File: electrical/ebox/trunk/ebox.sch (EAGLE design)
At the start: 160 parts, among them IC1 MAX3221CUE, IC10 SN74LVC1G125, IC11 MAX3221CUE, IC12 INA170, IC13 SN74LVC1G125, IC14 SN74LVC1G125, IC15 MAX3221CUE, IC16 MCP170333MB, IC17 SN74LVC1G125, IC18 SN74LVC1G125, IC19 74ALS04D, IC2 LT3652, IC3 XMEGA128A1, IC4 LT1161, IC5 SN74LVC1G125, IC6 SN74LVC1G125, IC7 MAX3221CUE, IC8 INA170, IC9 SN74LVC1G125, Q1 FDD4141TO252, U1 BLUETOOTH-RN42, U2 D2523T_, X1 7381-3PG-300, X10 DEANS-MALE, X11 B4B-ZR, X12 DEANS-MALE, X13 B4B-ZR, X14 22-23-2021, X15 DEANS-FEMALE, X16 DEANS-FEMALE, X17 USB_A, X2 7381-3PG-300, X3 7381-2PG-300, X4 17984-7PG-300, X5 17984-7PG-300, X6 17984-7PG-300, X7 17984-7PG-300, X8 22-23-2031, X9 22-23-2031

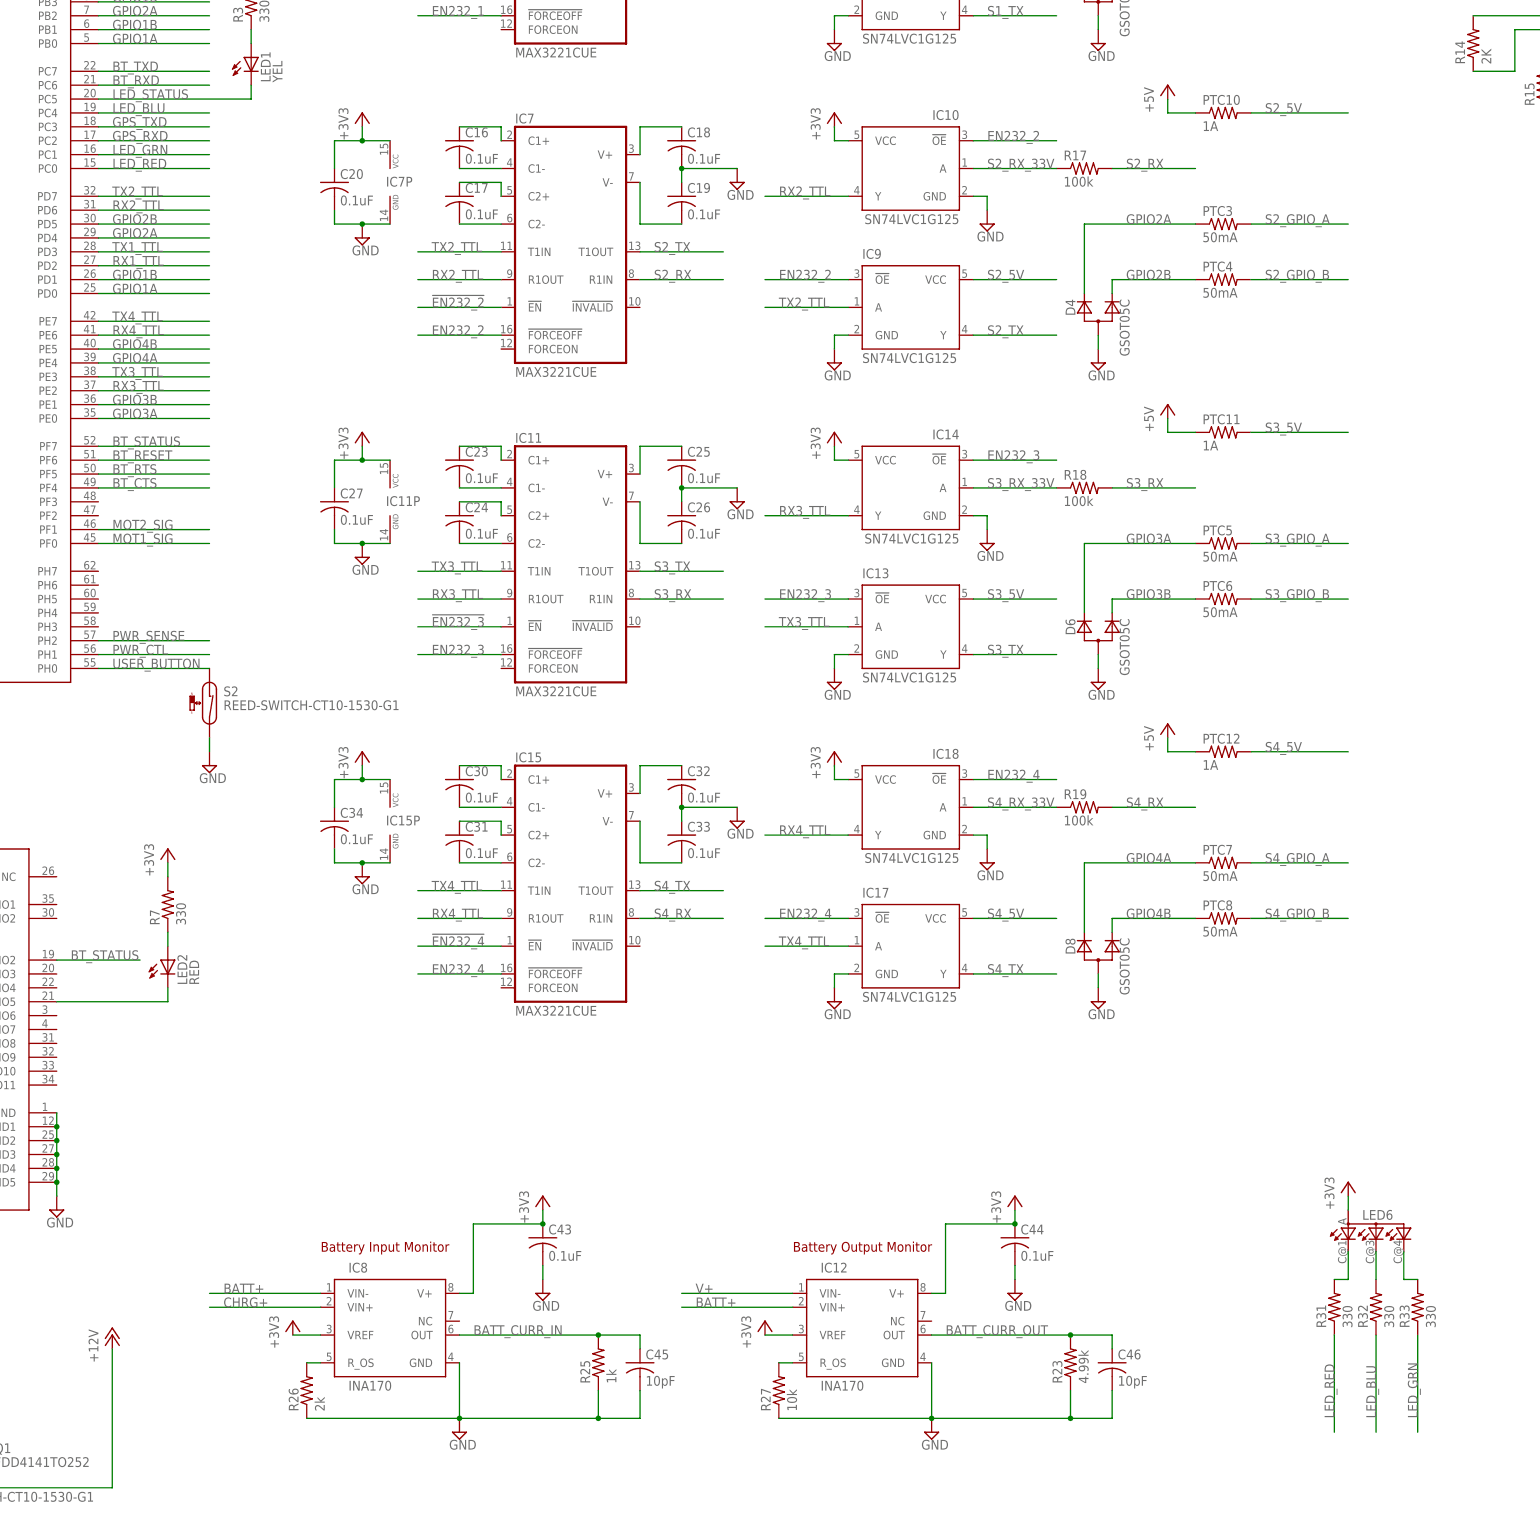
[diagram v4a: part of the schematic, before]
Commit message: Most of power layout is done too.
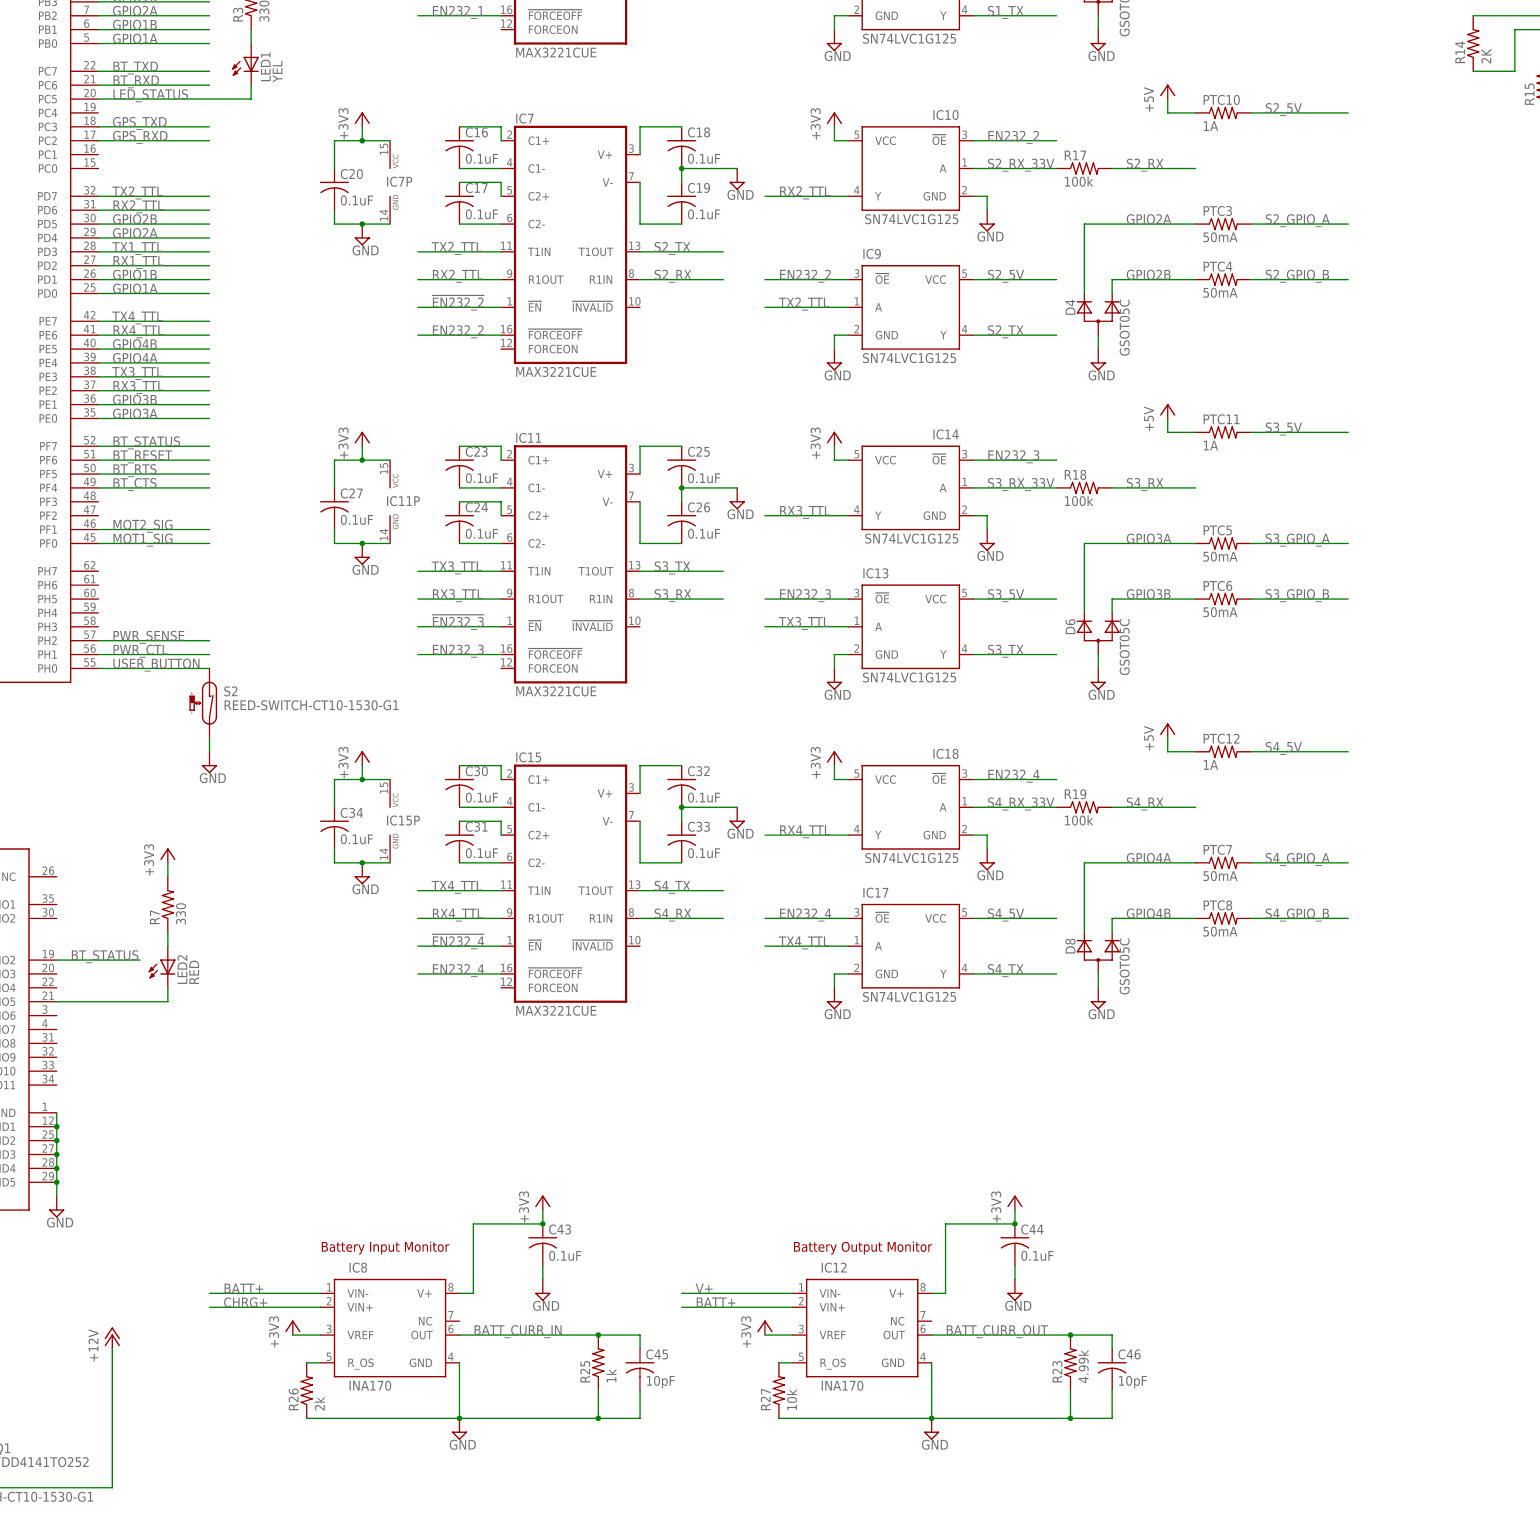
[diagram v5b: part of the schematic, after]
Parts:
- removed LED6: (no value), led:TOPLED-3P-LCC-4
- removed R31, R32, R33: 330, rcl:R-US_R0805
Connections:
- removed net LED_BLU: IC3.PC4, R32.1
- removed net LED_GRN: IC3.PC1, R33.1
- removed net LED_RED: IC3.PC0, R31.1
- removed net N$51: LED6.CBLUE, R32.2
- removed net N$52: LED6.CRED, R31.2
- removed net N$53: LED6.CGREEN, R33.2
- net +3V3: no longer LED6.A2
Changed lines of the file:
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@@
 <part name="SUPPLY3" library="supply2" deviceset="GND" device=""/>
 <part name="SUPPLY18" library="supply2" deviceset="GND" device=""/>
-<part name="LED6" library="led" deviceset="TOPLED-3" device="P-LCC-4"/>
-<part name="+3V21" library="supply1" deviceset="+3V3" device=""/>
-<part name="R31" library="rcl" deviceset="R-US_" device="R0805" value="330"/>
-<part name="R32" library="rcl" deviceset="R-US_" device="R0805" value="330"/>
-<part name="R33" library="rcl" deviceset="R-US_" device="R0805" value="330"/>
 <part name="X3" library="crw" deviceset="7381-2PG-300" device=""/>
 <part name="X4" library="crw" deviceset="17984-7PG-300" device=""/>
@@
 <instance part="SUPPLY3" gate="GND" x="393.7" y="261.62"/>
 <instance part="SUPPLY18" gate="GND" x="393.7" y="246.38"/>
-<instance part="LED6" gate="G$1" x="345.44" y="147.32"/>
-<instance part="+3V21" gate="G$1" x="340.36" y="157.48"/>
-<instance part="R31" gate="G$1" x="337.82" y="134.62" rot="R90"/>
-<instance part="R32" gate="G$1" x="345.44" y="134.62" rot="R90"/>
-<instance part="R33" gate="G$1" x="353.06" y="134.62" rot="R90"/>
 <instance part="X3" gate="-1" x="518.16" y="370.84"/>
 <instance part="X3" gate="-2" x="518.16" y="368.3"/>
@@
 </segment>
 <segment>
-<pinref part="+3V21" gate="G$1" pin="+3V3"/>
-<pinref part="LED6" gate="G$1" pin="A2"/>
-<wire x1="340.36" y1="154.94" x2="340.36" y2="152.4" width="0.1524" layer="91"/>
-</segment>
-<segment>
 <wire x1="81.28" y1="63.5" x2="86.36" y2="63.5" width="0.1524" layer="91"/>
 <pinref part="C28" gate="G$1" pin="1"/>
@@
 </segment>
 </net>
-<net name="LED_BLU" class="0">
-<segment>
-<pinref part="IC3" gate="G$1" pin="PC4"/>
-<wire x1="111.76" y1="353.06" x2="132.08" y2="353.06" width="0.1524" layer="91"/>
-<label x="114.3" y="353.06" size="1.778" layer="95"/>
-</segment>
-<segment>
-<wire x1="345.44" y1="129.54" x2="345.44" y2="111.76" width="0.1524" layer="91"/>
-<label x="345.44" y="114.3" size="1.778" layer="95" rot="R90"/>
-<pinref part="R32" gate="G$1" pin="1"/>
-</segment>
-</net>
-<net name="LED_RED" class="0">
-<segment>
-<pinref part="IC3" gate="G$1" pin="PC0"/>
-<wire x1="111.76" y1="342.9" x2="132.08" y2="342.9" width="0.1524" layer="91"/>
-<label x="114.3" y="342.9" size="1.778" layer="95"/>
-</segment>
-<segment>
-<pinref part="R31" gate="G$1" pin="1"/>
-<wire x1="337.82" y1="129.54" x2="337.82" y2="111.76" width="0.1524" layer="91"/>
-<label x="337.82" y="114.3" size="1.778" layer="95" rot="R90"/>
-</segment>
-</net>
-<net name="LED_GRN" class="0">
-<segment>
-<pinref part="IC3" gate="G$1" pin="PC1"/>
-<wire x1="111.76" y1="345.44" x2="132.08" y2="345.44" width="0.1524" layer="91"/>
-<label x="114.3" y="345.44" size="1.778" layer="95"/>
-</segment>
-<segment>
-<pinref part="R33" gate="G$1" pin="1"/>
-<wire x1="353.06" y1="129.54" x2="353.06" y2="111.76" width="0.1524" layer="91"/>
-<label x="353.06" y="114.3" size="1.778" layer="95" rot="R90"/>
-</segment>
-</net>
 <net name="N$6" class="0">
 <segment>
@@
 </segment>
 </net>
-<net name="N$51" class="0">
-<segment>
-<wire x1="345.44" y1="144.78" x2="345.44" y2="139.7" width="0.1524" layer="91"/>
-<pinref part="R32" gate="G$1" pin="2"/>
-<pinref part="LED6" gate="G$1" pin="CBLUE"/>
-</segment>
-</net>
-<net name="N$52" class="0">
-<segment>
-<pinref part="LED6" gate="G$1" pin="CRED"/>
-<wire x1="340.36" y1="144.78" x2="340.36" y2="139.7" width="0.1524" layer="91"/>
-<pinref part="R31" gate="G$1" pin="2"/>
-<wire x1="337.82" y1="139.7" x2="340.36" y2="139.7" width="0.1524" layer="91"/>
-</segment>
-</net>
-<net name="N$53" class="0">
-<segment>
-<pinref part="R33" gate="G$1" pin="2"/>
-<wire x1="353.06" y1="139.7" x2="350.52" y2="139.7" width="0.1524" layer="91"/>
-<pinref part="LED6" gate="G$1" pin="CGREEN"/>
-<wire x1="350.52" y1="139.7" x2="350.52" y2="144.78" width="0.1524" layer="91"/>
-</segment>
-</net>

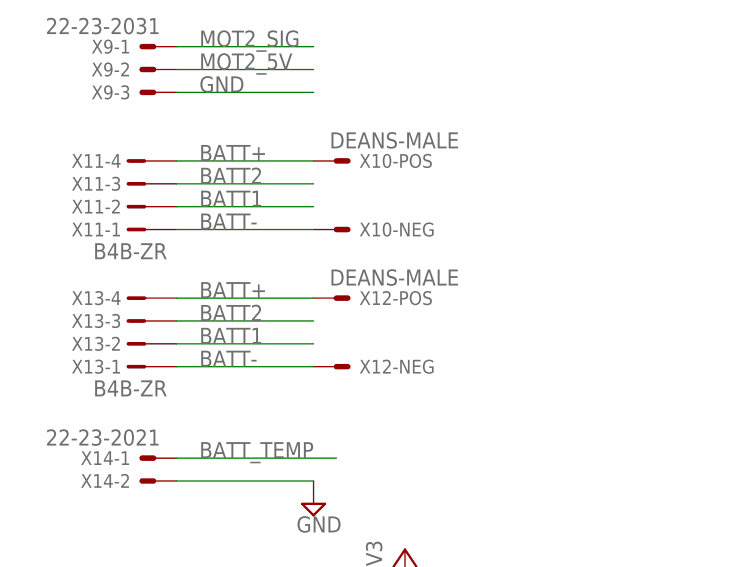
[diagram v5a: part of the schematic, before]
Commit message: Placed all components on board.
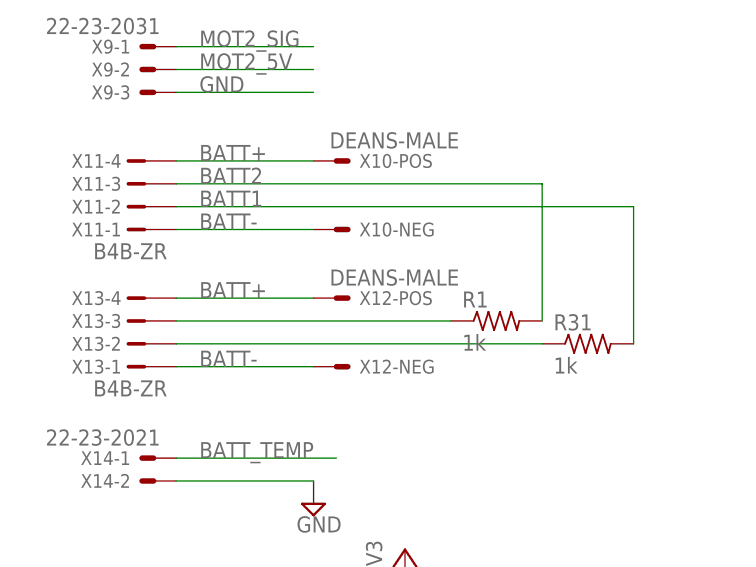
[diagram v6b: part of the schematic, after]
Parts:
- added R1, R31: 1k, rcl:R-US_R0805
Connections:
- new net N$46: R1.1, X13-3.1
- new net N$51: R31.1, X13-2.1
- net BATT1: now also R31.2; no longer X13-2.1
- net BATT2: now also R1.2; no longer X13-3.1
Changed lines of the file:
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@@
 <part name="T8" library="zetex" deviceset="NMOSSOT23-6" device=""/>
 <part name="T9" library="zetex" deviceset="NMOSSOT23-6" device=""/>
+<part name="R1" library="rcl" deviceset="R-US_" device="R0805" value="1k"/>
+<part name="R31" library="rcl" deviceset="R-US_" device="R0805" value="1k"/>
 </parts>
 <sheets>
@@
 <attribute name="NAME" x="454.66" y="368.3" size="1.778" layer="95" rot="R180"/>
 </instance>
+<instance part="R1" gate="G$1" x="535.94" y="220.98"/>
+<instance part="R31" gate="G$1" x="546.1" y="218.44"/>
 </instances>
 <busses>
@@
 <net name="BATT2" class="0">
 <segment>
-<wire x1="500.38" y1="236.22" x2="515.62" y2="236.22" width="0.1524" layer="91"/>
 <label x="502.92" y="236.22" size="1.778" layer="95"/>
 <pinref part="X11" gate="-3" pin="1"/>
-</segment>
-<segment>
-<wire x1="500.38" y1="220.98" x2="515.62" y2="220.98" width="0.1524" layer="91"/>
-<label x="502.92" y="220.98" size="1.778" layer="95"/>
-<pinref part="X13" gate="-3" pin="1"/>
+<pinref part="R1" gate="G$1" pin="2"/>
+<wire x1="541.02" y1="220.98" x2="541.02" y2="236.22" width="0.1524" layer="91"/>
+<wire x1="541.02" y1="236.22" x2="500.38" y2="236.22" width="0.1524" layer="91"/>
 </segment>
 </net>
 <net name="BATT1" class="0">
 <segment>
-<wire x1="500.38" y1="233.68" x2="515.62" y2="233.68" width="0.1524" layer="91"/>
 <label x="502.92" y="233.68" size="1.778" layer="95"/>
 <pinref part="X11" gate="-2" pin="1"/>
-</segment>
-<segment>
-<wire x1="500.38" y1="218.44" x2="515.62" y2="218.44" width="0.1524" layer="91"/>
-<label x="502.92" y="218.44" size="1.778" layer="95"/>
-<pinref part="X13" gate="-2" pin="1"/>
+<pinref part="R31" gate="G$1" pin="2"/>
+<wire x1="500.38" y1="233.68" x2="551.18" y2="233.68" width="0.1524" layer="91"/>
+<wire x1="551.18" y1="233.68" x2="551.18" y2="218.44" width="0.1524" layer="91"/>
 </segment>
 </net>
@@
 </segment>
 </net>
+<net name="N$46" class="0">
+<segment>
+<pinref part="X13" gate="-3" pin="1"/>
+<pinref part="R1" gate="G$1" pin="1"/>
+<wire x1="530.86" y1="220.98" x2="500.38" y2="220.98" width="0.1524" layer="91"/>
+</segment>
+</net>
+<net name="N$51" class="0">
+<segment>
+<pinref part="X13" gate="-2" pin="1"/>
+<pinref part="R31" gate="G$1" pin="1"/>
+<wire x1="541.02" y1="218.44" x2="500.38" y2="218.44" width="0.1524" layer="91"/>
+</segment>
+</net>

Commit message: Added rest of routing for much of power section.
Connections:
- removed net BATT-: X10-NEG.S, X11-1.1, X12-NEG.S, X13-1.1
- net FAULT1: now also IC3.PK7; no longer IC3.PK0
- net FAULT2: now also IC3.PK5; no longer IC3.PK2
- net FAULT3: now also IC3.PK3; no longer IC3.PK4
- net FAULT4: now also IC3.PK1; no longer IC3.PK6
- net GND: now also X10-NEG.S, X11-1.1, X12-NEG.S, X13-1.1
- net GPIO1A: now also D2.C2; no longer D2.C1
- net GPIO1B: now also D2.C1; no longer D2.C2
- net GPIO2A: now also D4.C2; no longer D4.C1
- net GPIO2B: now also D4.C1; no longer D4.C2
- net GPIO3A: now also D6.C2; no longer D6.C1
- net GPIO3B: now also D6.C1; no longer D6.C2
- net GPIO4A: now also D8.C2; no longer D8.C1
- net GPIO4B: now also D8.C1; no longer D8.C2
- net MOT1_SIG: now also IC3.PF1; no longer IC3.PF0
- net MOT2_SIG: now also IC3.PF0; no longer IC3.PF1
- net PWR_CTL1: now also IC3.PK6; no longer IC3.PK1
- net PWR_CTL2: now also IC3.PK4; no longer IC3.PK3
- net PWR_CTL3: now also IC3.PK2; no longer IC3.PK5
- net PWR_CTL4: now also IC3.PK0; no longer IC3.PK7

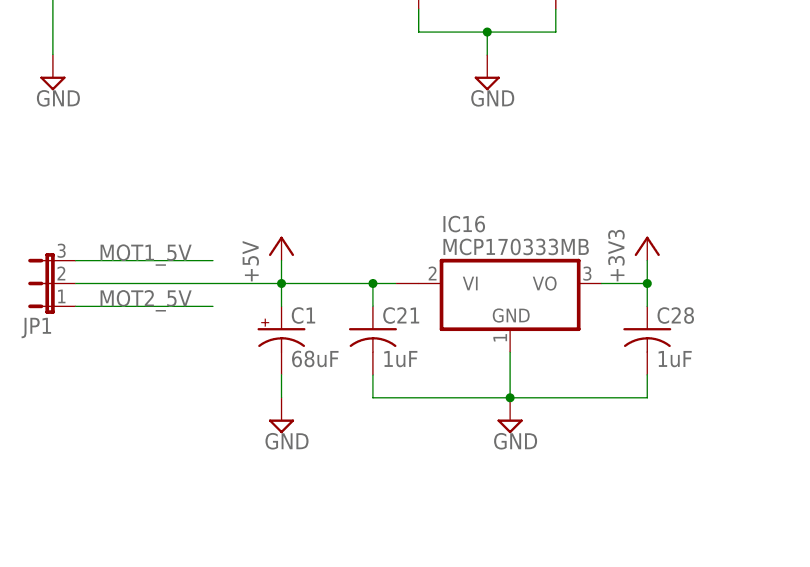
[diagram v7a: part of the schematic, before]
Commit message: Loads better routing of power.
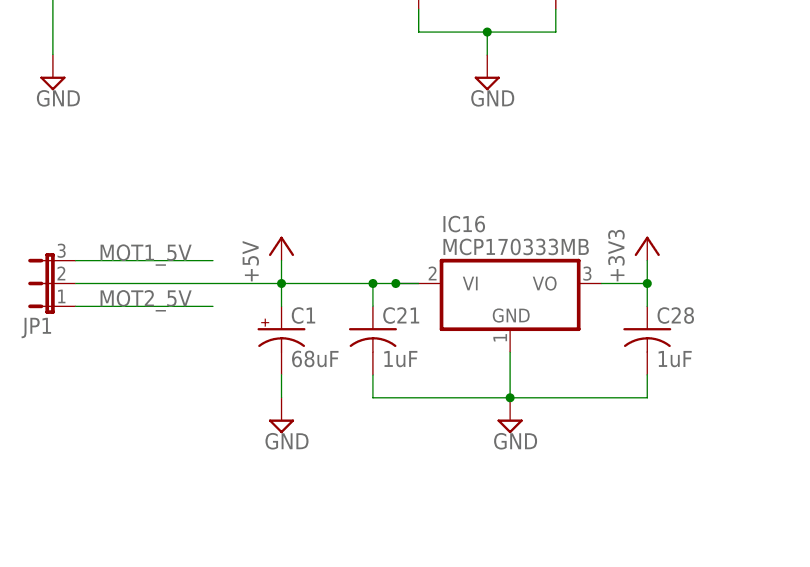
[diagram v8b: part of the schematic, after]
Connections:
- net +5V: now also IC16.VI
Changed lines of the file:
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@@
 <pinref part="IC16" gate="G$1" pin="VI1"/>
 <junction x="55.88" y="63.5"/>
+<pinref part="IC16" gate="G$1" pin="VI"/>
+<wire x1="58.42" y1="63.5" x2="60.96" y2="63.5" width="0.1524" layer="91"/>
+<junction x="58.42" y="63.5"/>
 </segment>
 <segment>
